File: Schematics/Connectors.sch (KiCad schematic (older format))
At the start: 106 parts, among them P601 CONN_02X05, P602 CONN_02X05, P603 CONN_02X05, P604 CONN_02X05, P605 CONN_02X05, P606 CONN_6X2, P607 CONN_02X05, P608 CONN_02X05, P609 CONN_02X20, P610 CONN_02X05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

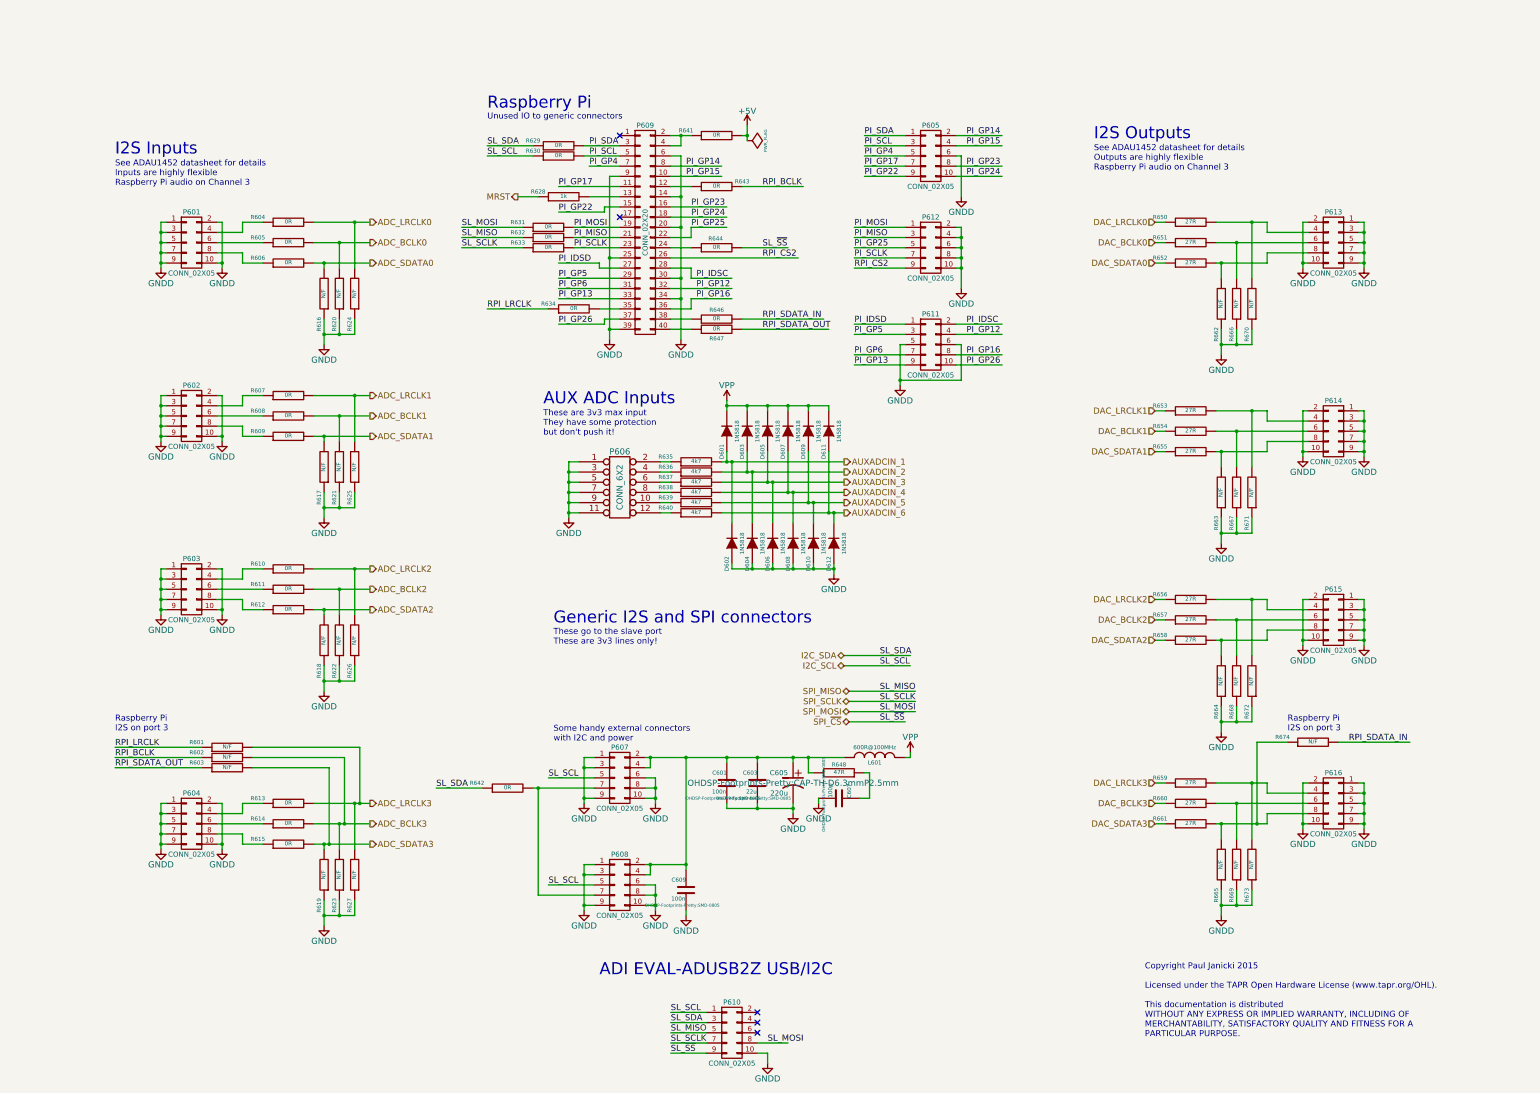
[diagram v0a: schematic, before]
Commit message: Adding ADAU1701 version
Because its easier...
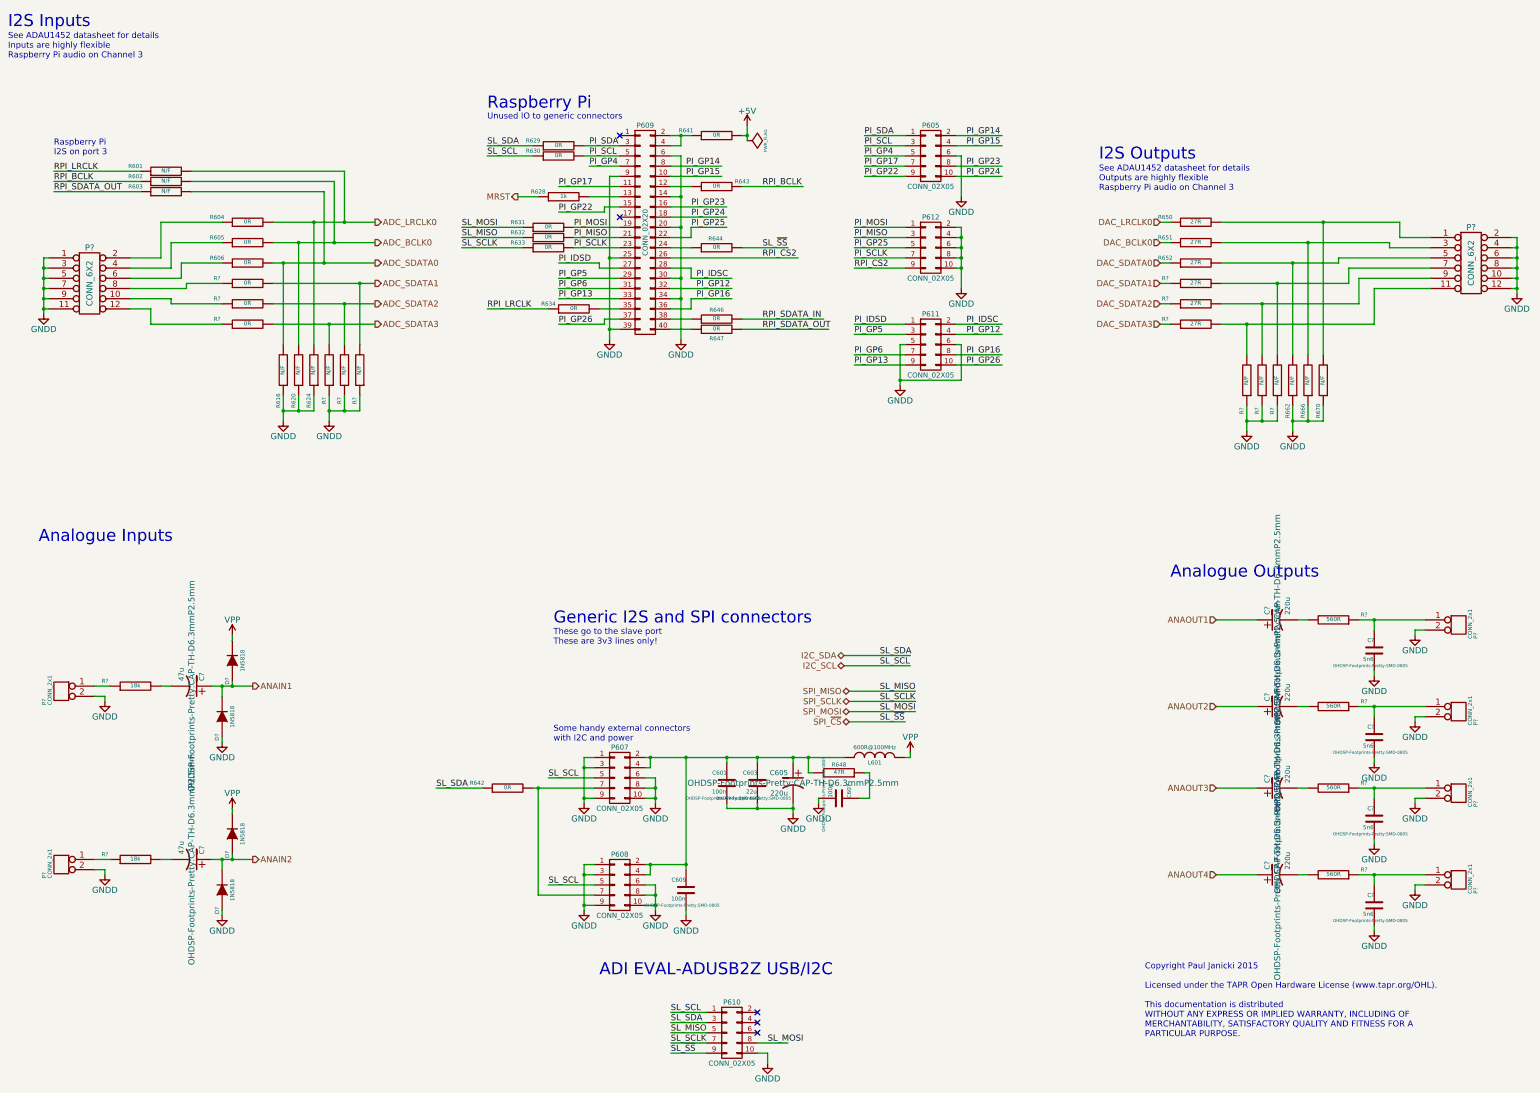
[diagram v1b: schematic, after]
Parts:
- removed D601, D602, D603, D604, D605, D606, D607, D608, D609, D610, D611, D612: 1N5818, OHDSP-Footprints-Pretty:DIODE-DO-41, symbol DIODE
- removed P601, P602, P603, P604, P613, P614, P615, P616: CONN_02X05, OHDSP-Footprints-Pretty:CONN_DIL_2X5, symbol CONN_02X05
- removed P606: CONN_6X2, OHDSP-Footprints-Pretty:CONN_DIL_2X6, symbol CONN_6X2
- removed R607, R608, R609, R610, R611, R612, R613, R614, R615: 0R, OHDSP-Footprints-Pretty:SMD-0603, symbol R
- removed R617, R618, R619, R621, R622, R623, R625, R626, R627, R663, R664, R665, R667, R668, R669, R671, R672, R673: N/F, OHDSP-Footprints-Pretty:SMD-0603, symbol R
- removed R635, R636, R637, R638, R639, R640: 4k7, OHDSP-Footprints-Pretty:SMD-0805, symbol R
- removed R653, R654, R655, R656, R657, R658, R659, R660, R661: 27R, OHDSP-Footprints-Pretty:SMD-0603, symbol R
- removed R674: N/F, OHDSP-Footprints-Pretty:SMD-0805, symbol R
- added C? (x2): 47u, OHDSP-Footprints-Pretty:CAP-TH-D6.3mmP2.5mm, symbol CP1
- added C? (x4): 220u, OHDSP-Footprints-Pretty:CAP-TH-D6.3mmP2.5mm, symbol CP1
- added C? (x4): 5n6, OHDSP-Footprints-Pretty:SMD-0805, symbol C
- added D? (x4): 1N5818, OHDSP-Footprints-Pretty:DIODE-DO-41, symbol DIODE
- added P? (x2): CONN_6X2, symbol CONN_6X2
- added P? (x6): CONN_2x1, symbol CONN_2x1
- added R? (x3): 0R, OHDSP-Footprints-Pretty:SMD-0603, symbol R
- added R? (x6): N/F, OHDSP-Footprints-Pretty:SMD-0603, symbol R
- added R? (x3): 27R, OHDSP-Footprints-Pretty:SMD-0603, symbol R
- added R? (x2): 18k, OHDSP-Footprints-Pretty:SMD-0805, symbol R
- added R? (x4): 560R, OHDSP-Footprints-Pretty:SMD-0805, symbol R
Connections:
- net labels added: ANAIN1, ANAIN2, ANAOUT1, ANAOUT2, ANAOUT3, ANAOUT4
- net labels removed: ADC_BCLK1, ADC_BCLK2, ADC_BCLK3, ADC_LRCLK1, ADC_LRCLK2, ADC_LRCLK3, AUXADCIN_1, AUXADCIN_2, AUXADCIN_3, AUXADCIN_4, AUXADCIN_5, AUXADCIN_6, DAC_BCLK1, DAC_BCLK2, DAC_BCLK3, DAC_LRCLK1, DAC_LRCLK2, DAC_LRCLK3
- wire segments 425 -> 305
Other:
- note added: "Analogue Inputs"
- note added: "Analogue Outputs"
- note removed: "AUX ADC Inputs"
- note removed: "These are 3v3 max input\nThey have some protection\nbut don't push it!"
- moved on the sheet: R601, R602, R603, R604, R605, R606, R616, R620, R624, R650, R651, R652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

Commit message: WIP
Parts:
- removed P? (x2): CONN_6X2, symbol CONN_6X2
- removed R631, R632, R633, R642, R644: 0R, OHDSP-Footprints-Pretty:SMD-0805, symbol R
- added P? (x2): CONN_02X10, symbol CONN_02X10
- added R?: 0R, OHDSP-Footprints-Pretty:SMD-0603, symbol R
- added R? (x2): N/F, OHDSP-Footprints-Pretty:SMD-0603, symbol R
- added R?: 27R, OHDSP-Footprints-Pretty:SMD-0603, symbol R
- added R?: N/F, OHDSP-Footprints-Pretty:SMD-0805, symbol R
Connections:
- net labels added: ADC_MCLK, DAC_MCLK, PI_CS1, PI_CS2
- net labels removed: RPI_CS2, SPI_MISO, SPI_MOSI, SPI_SCLK, SPI_~CS
- wire segments 305 -> 314
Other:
- note added: "Allow Raspberry Pi audio"
- note removed: "Raspberry Pi\nI2S on port 3"
- note removed: "See ADAU1452 datasheet for details\nInputs are highly flexible\nRaspberry Pi audio on Channel 3"
- note removed: "See ADAU1452 datasheet for details\nOutputs are highly flexible\nRaspberry Pi audio on Channel 3"
- moved on the sheet: C601, C603, C605, C607, C609, C?, D?, L601, P605, P607, P608, P609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

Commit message: WIP
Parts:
- added R? (x2): 0R, OHDSP-Footprints-Pretty:SMD-0603, symbol R
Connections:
- net labels added: ADC_RESET, DAC_RESET
- wire segments 314 -> 322
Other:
- moved on the sheet: R616, R620, R624, R?
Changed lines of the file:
@@
 $Descr A3 16535 11693
 encoding utf-8
-Sheet 5 6
+Sheet 5 5
 Title ""
 Date "10 feb 2015"
@@
 L R R616
 U 1 1 54DCE22D
-P 2950 3250
-F 0 "R616" V 3000 3550 40  0000 C CNN
-F 1 "N/F" V 2957 3251 40  0000 C CNN
-F 2 "OHDSP-Footprints-Pretty:SMD-0603" V 2880 3250 30  0001 C CNN
-F 3 "~" H 2950 3250 30  0000 C CNN
-	1    2950 3250
+P 2950 3400
+F 0 "R616" V 3000 3700 40  0000 C CNN
+F 1 "N/F" V 2957 3401 40  0000 C CNN
+F 2 "OHDSP-Footprints-Pretty:SMD-0603" V 2880 3400 30  0001 C CNN
+F 3 "~" H 2950 3400 30  0000 C CNN
+	1    2950 3400
 	-1   0    0    1
 $EndComp
@@
 L R R620
 U 1 1 54DCE23F
-P 3100 3250
-F 0 "R620" V 3150 3550 40  0000 C CNN
-F 1 "N/F" V 3107 3251 40  0000 C CNN
-F 2 "OHDSP-Footprints-Pretty:SMD-0603" V 3030 3250 30  0001 C CNN
-F 3 "~" H 3100 3250 30  0000 C CNN
-	1    3100 3250
+P 3100 3400
+F 0 "R620" V 3150 3700 40  0000 C CNN
+F 1 "N/F" V 3107 3401 40  0000 C CNN
+F 2 "OHDSP-Footprints-Pretty:SMD-0603" V 3030 3400 30  0001 C CNN
+F 3 "~" H 3100 3400 30  0000 C CNN
+	1    3100 3400
 	-1   0    0    1
 $EndComp
@@
 L R R624
 U 1 1 54DCE245
-P 3250 3250
-F 0 "R624" V 3300 3550 40  0000 C CNN
-F 1 "N/F" V 3257 3251 40  0000 C CNN
-F 2 "OHDSP-Footprints-Pretty:SMD-0603" V 3180 3250 30  0001 C CNN
-F 3 "~" H 3250 3250 30  0000 C CNN
-	1    3250 3250
+P 3250 3400
+F 0 "R624" V 3300 3700 40  0000 C CNN
+F 1 "N/F" V 3257 3401 40  0000 C CNN
+F 2 "OHDSP-Footprints-Pretty:SMD-0603" V 3180 3400 30  0001 C CNN
+F 3 "~" H 3250 3400 30  0000 C CNN
+	1    3250 3400
 	-1   0    0    1
 $EndComp
@@
 L GNDD #PWR0108
 U 1 1 54DCE262
-P 2950 3750
-F 0 "#PWR0108" H 2950 3500 60  0001 C CNN
-F 1 "GNDD" H 2950 3600 60  0000 C CNN
-F 2 "" H 2950 3750 60  0000 C CNN
-F 3 "" H 2950 3750 60  0000 C CNN
-	1    2950 3750
+P 2950 3900
+F 0 "#PWR0108" H 2950 3650 60  0001 C CNN
+F 1 "GNDD" H 2950 3750 60  0000 C CNN
+F 2 "" H 2950 3900 60  0000 C CNN
+F 3 "" H 2950 3900 60  0000 C CNN
+	1    2950 3900
 	1    0    0    -1
 $EndComp
@@
 Connection ~ 14650 2100
 Wire Wire Line
-	14600 2100 14650 2100
+	14650 2100 14600 2100
 Connection ~ 14650 2200
 Wire Wire Line
@@
 	800  6950 1250 6950
 Wire Wire Line
-	3250 1800 3250 3000
+	3250 1800 3250 3150
 Connection ~ 11800 1450
 Wire Wire Line
@@
 	2850 2000 3850 2000
 Wire Wire Line
-	3100 2000 3100 3000
+	3100 2000 3100 3150
 Connection ~ 2950 2200
 Wire Wire Line
 	2850 2200 3850 2200
 Wire Wire Line
-	2950 2200 2950 3000
+	2950 2200 2950 3150
 Connection ~ 900  2750
 Wire Wire Line
@@
 	700  1500 1550 1500
 Wire Wire Line
-	2950 3500 2950 3750
-Connection ~ 3100 3650
-Wire Wire Line
-	3250 3650 3250 3500
-Connection ~ 2950 3650
-Wire Wire Line
-	2950 3650 3250 3650
-Wire Wire Line
-	3100 3500 3100 3650
+	2950 3650 2950 3900
+Connection ~ 3100 3800
+Wire Wire Line
+	3250 3800 3250 3650
+Connection ~ 2950 3800
+Wire Wire Line
+	2950 3800 3250 3800
+Wire Wire Line
+	3100 3650 3100 3800
 Wire Wire Line
 	10850 1550 11200 1550
@@
 L R R?
 U 1 1 55149D86
-P 3400 3250
-F 0 "R?" V 3450 3550 40  0000 C CNN
-F 1 "N/F" V 3407 3251 40  0000 C CNN
-F 2 "OHDSP-Footprints-Pretty:SMD-0603" V 3330 3250 30  0001 C CNN
-F 3 "~" H 3400 3250 30  0000 C CNN
-	1    3400 3250
+P 3400 3400
+F 0 "R?" V 3450 3700 40  0000 C CNN
+F 1 "N/F" V 3407 3401 40  0000 C CNN
+F 2 "OHDSP-Footprints-Pretty:SMD-0603" V 3330 3400 30  0001 C CNN
+F 3 "~" H 3400 3400 30  0000 C CNN
+	1    3400 3400
 	-1   0    0    1
 $EndComp
@@
 L R R?
 U 1 1 55149D8C
-P 3550 3250
-F 0 "R?" V 3600 3550 40  0000 C CNN
-F 1 "N/F" V 3557 3251 40  0000 C CNN
-F 2 "OHDSP-Footprints-Pretty:SMD-0603" V 3480 3250 30  0001 C CNN
-F 3 "~" H 3550 3250 30  0000 C CNN
-	1    3550 3250
+P 3550 3400
+F 0 "R?" V 3600 3700 40  0000 C CNN
+F 1 "N/F" V 3557 3401 40  0000 C CNN
+F 2 "OHDSP-Footprints-Pretty:SMD-0603" V 3480 3400 30  0001 C CNN
+F 3 "~" H 3550 3400 30  0000 C CNN
+	1    3550 3400
 	-1   0    0    1
 $EndComp
@@
 L R R?
 U 1 1 55149D92
-P 3700 3250
-F 0 "R?" V 3750 3550 40  0000 C CNN
-F 1 "N/F" V 3707 3251 40  0000 C CNN
-F 2 "OHDSP-Footprints-Pretty:SMD-0603" V 3630 3250 30  0001 C CNN
-F 3 "~" H 3700 3250 30  0000 C CNN
-	1    3700 3250
+P 3700 3400
+F 0 "R?" V 3750 3700 40  0000 C CNN
+F 1 "N/F" V 3707 3401 40  0000 C CNN
+F 2 "OHDSP-Footprints-Pretty:SMD-0603" V 3630 3400 30  0001 C CNN
+F 3 "~" H 3700 3400 30  0000 C CNN
+	1    3700 3400
 	-1   0    0    1
 $EndComp
@@
 L GNDD #PWR?
 U 1 1 55149DF3
-P 3400 3750
-F 0 "#PWR?" H 3400 3500 60  0001 C CNN
-F 1 "GNDD" H 3400 3600 60  0000 C CNN
-F 2 "" H 3400 3750 60  0000 C CNN
-F 3 "" H 3400 3750 60  0000 C CNN
-	1    3400 3750
-	1    0    0    -1
-$EndComp
-Wire Wire Line
-	3400 3500 3400 3750
-Connection ~ 3550 3650
-Wire Wire Line
-	3700 3650 3700 3500
-Connection ~ 3400 3650
-Wire Wire Line
-	3400 3650 3700 3650
-Wire Wire Line
-	3550 3500 3550 3650
+P 3400 3900
+F 0 "#PWR?" H 3400 3650 60  0001 C CNN
+F 1 "GNDD" H 3400 3750 60  0000 C CNN
+F 2 "" H 3400 3900 60  0000 C CNN
+F 3 "" H 3400 3900 60  0000 C CNN
+	1    3400 3900
+	1    0    0    -1
+$EndComp
+Wire Wire Line
+	3400 3650 3400 3900
+Connection ~ 3550 3800
+Wire Wire Line
+	3700 3800 3700 3650
+Connection ~ 3400 3800
+Wire Wire Line
+	3400 3800 3700 3800
+Wire Wire Line
+	3550 3650 3550 3800
 Wire Wire Line
 	2850 2400 3850 2400
@@
 	2850 2800 3850 2800
 Wire Wire Line
-	3400 3000 3400 2800
+	3400 3150 3400 2800
 Connection ~ 3400 2800
 Wire Wire Line
-	3550 3000 3550 2600
+	3550 3150 3550 2600
 Connection ~ 3550 2600
 Wire Wire Line
-	3700 3000 3700 2400
+	3700 3150 3700 2400
 Connection ~ 3700 2400
 Wire Wire Line
@@
 L R R?
 U 1 1 55143882
-P 2150 3200
-F 0 "R?" V 2200 3500 40  0000 C CNN
-F 1 "N/F" V 2157 3201 40  0000 C CNN
-F 2 "OHDSP-Footprints-Pretty:SMD-0603" V 2080 3200 30  0001 C CNN
-F 3 "~" H 2150 3200 30  0000 C CNN
-	1    2150 3200
+P 2150 3350
+F 0 "R?" V 2200 3650 40  0000 C CNN
+F 1 "N/F" V 2157 3351 40  0000 C CNN
+F 2 "OHDSP-Footprints-Pretty:SMD-0603" V 2080 3350 30  0001 C CNN
+F 3 "~" H 2150 3350 30  0000 C CNN
+	1    2150 3350
 	-1   0    0    1
 $EndComp
 Wire Wire Line
-	2150 2950 2150 1600
+	2150 3100 2150 1600
 Connection ~ 2150 1600
 $Comp
 L GNDD #PWR?
 U 1 1 55143B7B
-P 2150 3750
-F 0 "#PWR?" H 2150 3500 60  0001 C CNN
-F 1 "GNDD" H 2150 3600 60  0000 C CNN
-F 2 "" H 2150 3750 60  0000 C CNN
-F 3 "" H 2150 3750 60  0000 C CNN
-	1    2150 3750
-	1    0    0    -1
-$EndComp
-Wire Wire Line
-	2150 3750 2150 3450
+P 2150 3900
+F 0 "#PWR?" H 2150 3650 60  0001 C CNN
+F 1 "GNDD" H 2150 3750 60  0000 C CNN
+F 2 "" H 2150 3900 60  0000 C CNN
+F 3 "" H 2150 3900 60  0000 C CNN
+	1    2150 3900
+	1    0    0    -1
+$EndComp
+Wire Wire Line
+	2150 3900 2150 3600
 $Comp
 L CONN_02X10 P?
@@
 Connection ~ 14650 2000
 Connection ~ 14650 2900
+Text HLabel 5300 3000 0    60   Input ~ 0
+DAC_RESET
+$Comp
+L R R?
+U 1 1 5516B3D2
+P 5650 3000
+F 0 "R?" V 5700 3300 40  0000 C CNN
+F 1 "0R" V 5657 3001 40  0000 C CNN
+F 2 "OHDSP-Footprints-Pretty:SMD-0603" V 5580 3000 30  0001 C CNN
+F 3 "~" H 5650 3000 30  0000 C CNN
+	1    5650 3000
+	0    -1   -1   0
+$EndComp
+Wire Wire Line
+	5900 3000 7550 3000
+Wire Wire Line
+	7550 3000 7550 2650
+Wire Wire Line
+	7550 2650 7950 2650
+Wire Wire Line
+	5400 3000 5300 3000
+Text HLabel 3850 3000 2    60   Input ~ 0
+ADC_RESET
+Wire Wire Line
+	1600 3000 1600 2850
+Wire Wire Line
+	1600 2850 1450 2850
+$Comp
+L R R?
+U 1 1 5516C7B3
+P 2600 3000
+F 0 "R?" V 2650 3300 40  0000 C CNN
+F 1 "0R" V 2607 3001 40  0000 C CNN
+F 2 "OHDSP-Footprints-Pretty:SMD-0603" V 2530 3000 30  0001 C CNN
+F 3 "~" H 2600 3000 30  0000 C CNN
+	1    2600 3000
+	0    -1   -1   0
+$EndComp
+Wire Wire Line
+	2850 3000 3850 3000
+Wire Wire Line
+	2350 3000 1600 3000
 $EndSCHEMATC

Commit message: WIP
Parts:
- C501: renamed from C609; footprint OHDSP-Footprints-Pretty:SMD-0805 -> (none)
- C502: renamed from C601; footprint OHDSP-Footprints-Pretty:SMD-0805 -> (none)
- C503: renamed from C603; footprint OHDSP-Footprints-Pretty:SMD-0805 -> (none)
- C504: renamed from C605; footprint OHDSP-Footprints-Pretty:CAP-TH-D6.3mmP2.5mm -> (none)
- C505: renamed from C607; footprint OHDSP-Footprints-Pretty:SMD-0805 -> (none)
- C506, C507, C508, C509, C510, C511: renamed from C?; footprint OHDSP-Footprints-Pretty:CAP-TH-D6.3mmP2.5mm -> (none)
- C512, C513, C514, C515: renamed from C?; footprint OHDSP-Footprints-Pretty:SMD-0805 -> (none)
- D501, D502, D503, D504: renamed from D?; footprint OHDSP-Footprints-Pretty:DIODE-DO-41 -> (none)
- L501: renamed from L601; footprint OHDSP-Footprints-Pretty:SMD-0805 -> (none)
- P502: renamed from P607; footprint OHDSP-Footprints-Pretty:CONN_DIL_2X5 -> (none)
- P503: renamed from P608; footprint OHDSP-Footprints-Pretty:CONN_DIL_2X5 -> (none)
- P504: renamed from P610; footprint OHDSP-Footprints-Pretty:CONN_DIL_2X5 -> (none)
- P508: renamed from P609; footprint OHDSP-Footprints-Pretty:CONN_DIL_2X20 -> (none)
- P509: renamed from P605; footprint OHDSP-Footprints-Pretty:CONN_DIL_2X5 -> (none)
- P510: renamed from P612; footprint OHDSP-Footprints-Pretty:CONN_DIL_2X5 -> (none)
- P511: renamed from P611; footprint OHDSP-Footprints-Pretty:CONN_DIL_2X5 -> (none)
- R501: renamed from R601; footprint OHDSP-Footprints-Pretty:SMD-0805 -> (none)
- R502: renamed from R602; footprint OHDSP-Footprints-Pretty:SMD-0805 -> (none)
- R503: renamed from R603; footprint OHDSP-Footprints-Pretty:SMD-0805 -> (none)
- R504, R505, R509, R510, R511, R512, R516, R517, R519, R520, R524, R525, R526, R527, R529, R530, R531, R535: renamed from R?; footprint OHDSP-Footprints-Pretty:SMD-0603 -> (none)
- R506: renamed from R604; footprint OHDSP-Footprints-Pretty:SMD-0603 -> (none)
- R507: renamed from R605; footprint OHDSP-Footprints-Pretty:SMD-0603 -> (none)
- R508: renamed from R606; footprint OHDSP-Footprints-Pretty:SMD-0603 -> (none)
- R513: renamed from R616; footprint OHDSP-Footprints-Pretty:SMD-0603 -> (none)
- R514: renamed from R620; footprint OHDSP-Footprints-Pretty:SMD-0603 -> (none)
- R515: renamed from R624; footprint OHDSP-Footprints-Pretty:SMD-0603 -> (none)
- R518: renamed from R648; footprint OHDSP-Footprints-Pretty:SMD-0805 -> (none)
- R521: renamed from R650; footprint OHDSP-Footprints-Pretty:SMD-0603 -> (none)
- R522: renamed from R651; footprint OHDSP-Footprints-Pretty:SMD-0603 -> (none)
- R523: renamed from R652; footprint OHDSP-Footprints-Pretty:SMD-0603 -> (none)
- R528, R536, R537, R546, R547, R548, R549: renamed from R?; footprint OHDSP-Footprints-Pretty:SMD-0805 -> (none)
- R532: renamed from R662; footprint OHDSP-Footprints-Pretty:SMD-0603 -> (none)
- R533: renamed from R666; footprint OHDSP-Footprints-Pretty:SMD-0603 -> (none)
- R534: renamed from R670; footprint OHDSP-Footprints-Pretty:SMD-0603 -> (none)
- R538: renamed from R629; footprint OHDSP-Footprints-Pretty:SMD-0805 -> (none)
- R539: renamed from R630; footprint OHDSP-Footprints-Pretty:SMD-0805 -> (none)
- R540: renamed from R628; footprint OHDSP-Footprints-Pretty:SMD-0805 -> (none)
- R541: renamed from R634; footprint OHDSP-Footprints-Pretty:SMD-0805 -> (none)
- R542: renamed from R641; footprint OHDSP-Footprints-Pretty:SMD-0805 -> (none)
- R543: renamed from R643; footprint OHDSP-Footprints-Pretty:SMD-0805 -> (none)
- R544: renamed from R646; footprint OHDSP-Footprints-Pretty:SMD-0805 -> (none)
- R545: renamed from R647; footprint OHDSP-Footprints-Pretty:SMD-0805 -> (none)
- gave numbers to parts that had none: 8
